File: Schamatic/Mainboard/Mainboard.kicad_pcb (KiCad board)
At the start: 2 copper layers, 45 x 120 mm, 77 parts, among them J1 CONN_01X02, J2 CONN_01X02, J3 CONN_01X02, J4 CONN_01X02, J5 CONN_01X02, J6 CONN_02X05, J7 CONN_02X20, J8 CONN_01X02, J9 CONN_01X02, Q1 Q_NMOS_GDS, Q2 PSMN014-40YS, U1 IFX91041 - 3.3V, U2 IFX91041 - 5V, U3 MC78M00, U4 LM5122, U5 UCC27611, U6 ACS781, U7 LSM6DS33, U8 STM32F031G6U6, U9 LTC2876, Y1 Resonator_Small

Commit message: 3d updates for new controller
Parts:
- added C23: 0.1uF, Capacitors_SMD:C_0603, F.Cu at (70.3, 62.1)
- added R21: 10k, Resistors_SMD:R_0603, F.Cu at (65.0, 63.3)
- moved R15 191.4 mm to (52.5, 71.6)
- moved D3 189.6 mm to (78.5, 103.0), turned to 270 degrees
- moved R16 177.6 mm to (52.6, 73.9)
- moved R17 155.6 mm to (90.5, 118.8)
- moved C2 154.2 mm to (60.2, 104.8)
- moved D1 143.2 mm to (52.9, 100.0), turned to 90 degrees
- moved R18 142.8 mm to (90.5, 120.7), turned to 180 degrees
- moved Y1 140.9 mm to (57.2, 79.9), turned to 270 degrees
- moved L1 140.9 mm to (52.8, 95.4), turned to 270 degrees
- moved C13 138.5 mm to (72.7, 92.8)
- moved L2 134.6 mm to (67.1, 94.3), turned to 90 degrees
- moved R2 111.0 mm to (57.2, 104.8)
- moved C21 110.0 mm to (90.5, 122.7), turned to 180 degrees
- moved C7 109.6 mm to (53.8, 104.9), turned to 180 degrees
- moved R3 104.5 mm to (72.3, 103.9)
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
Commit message: continue working on mainboard
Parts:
- added C24: 0.1uF, Capacitors_SMD:C_0603, F.Cu at (61.1, 64.8)
- added C25: 0.1uF, Capacitors_SMD:C_0603, F.Cu at (71.8, 72.4)
- added C26: 0.1uF, Capacitors_SMD:C_0603, F.Cu at (59.4, 73.0)
- added C27: 2.2uF, Capacitors_SMD:C_0603, F.Cu at (88.8, 106.0)
- added J10: CONN_01X04, Pin_Headers:Pin_Header_Straight_1x04_Pitch2.54mm, F.Cu at (59.8, 46.0)
- added U10: LTC2954, Dizzy:8-DFN-DDB, F.Cu at (92.8, 107.2)
- R4: value 83k -> 10k
- R5: value 10k -> 390
- moved R5 94.8 mm to (62.4, 49.5), turned to 270 degrees
- moved R4 51.1 mm to (90.9, 105.8), turned to 270 degrees
- moved C7 25.9 mm to (77.6, 94.9), turned to 270 degrees
- moved D3 23.6 mm to (54.9, 103.4), turned to 180 degrees
- moved J9 22.6 mm to (52.2, 84.9), turned to 0 degrees
- moved D1 22.1 mm to (73.7, 92.5), turned to 0 degrees
- moved R2 20.7 mm to (78.0, 104.8), turned to 180 degrees
- moved C9 19.6 mm to (58.5, 103.4), turned to 180 degrees
- moved C2 17.8 mm to (78.0, 103.2)
- moved U1 17.2 mm to (75.1, 99.5), turned to 180 degrees
- moved J6 17.0 mm to (77.7, 65.1)
- moved L1 16.5 mm to (69.2, 97.4), turned to 90 degrees
- moved C12 15.8 mm to (73.4, 95.1)
- moved C13 15.0 mm to (57.8, 94.7)
- moved J1 14.1 mm to (80.8, 46.0)
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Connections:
- J7 pad 16: (no net) -> GPIO16
- J7 pad 18: (no net) -> GPIO18
- J7 pad 33: GPIO13 -> (no net)
- J7 pad 38: GPIO20 -> PWR_INT
- J7 pad 40: GPIO21 -> ~PWR_KILL
- R4 pad 1: +BATT -> 3.3V
- R4 pad 2: Net-(R4-Pad2) -> ~PWR_KILL
- R5 pad 1: Net-(R4-Pad2) -> Net-(J10-Pad2)
- R5 pad 2: Earth -> 3.3V
- U1 pad 7: Net-(C10-Pad2) -> PWR_EN
- U2 pad 7: Net-(C9-Pad2) -> PWR_EN
- U4 pad 6: Net-(R4-Pad2) -> PWR_EN
- U8 pad 1: (no net) -> 3.3V
- U8 pad 14: GPIO13 -> V_ADC
- U8 pad 17: (no net) -> 3.3V
- U8 pad 25: GPIO21 -> GPIO18
- U8 pad 26: GPIO20 -> GPIO16
- U8 pad 6: (no net) -> I_ADC
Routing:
- net 3.3V: track 0.00 -> 263.8 mm, vias 0 -> 17
- net PWR_EN: track 0.00 -> 95.8 mm, vias 0 -> 5
- net GPIO16: track 0.00 -> 92.4 mm, vias 0 -> 4
- net +BATT: track 120.7 -> 198.9 mm, vias 4 -> 12
- net PWR_BUTTON: track 0.00 -> 75.2 mm, vias 0 -> 1
- net I_ADC: track 0.00 -> 67.2 mm, vias 0 -> 2
- net RECVRDY: track 0.00 -> 57.8 mm, vias 0 -> 2
- net V_ADC: track 0.00 -> 57.7 mm, vias 0 -> 2
- net RESPRDY: track 0.00 -> 56.7 mm, vias 0 -> 2
- net GPIO18: track 0.00 -> 43.1 mm, vias 0 -> 2
- net GPIO26: track 0.00 -> 38.9 mm
- net SCL: track 0.00 -> 38.2 mm, vias 0 -> 3
- net GPIO19: track 0.00 -> 35.7 mm
- net Net-(R17-Pad1): track 0.00 -> 34.2 mm
- net SDA: track 0.00 -> 33.9 mm, vias 0 -> 3
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- added copper zone on F.Cu, net +90V
- added copper zone on F.Cu, net +BATT
- added copper zone on B.Cu, net 3.3V
- added copper zone on F.Cu, net 3.3V
- added copper zone on B.Cu, net 5V
- added copper zone on F.Cu, net 5V
- added copper zone on B.Cu, net Earth
- added copper zone on F.Cu, net Earth
- added copper zone on F.Cu, net Net-(C15-Pad1)
- added copper zone on F.Cu, net Net-(C17-Pad1)
- added copper zone on F.Cu, net Net-(L3-Pad1)
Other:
- board size 45 x 120 mm -> 45 x 130 mm

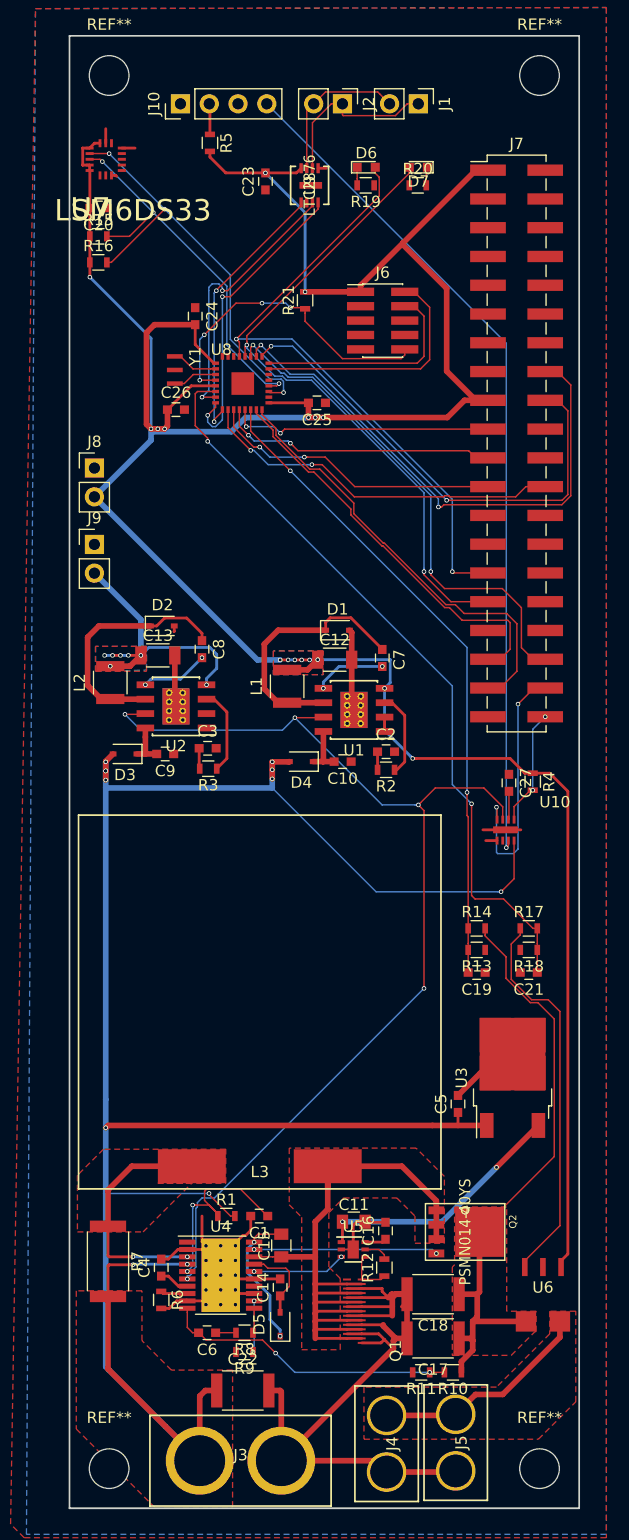
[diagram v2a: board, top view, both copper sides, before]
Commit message: bigger current regulators
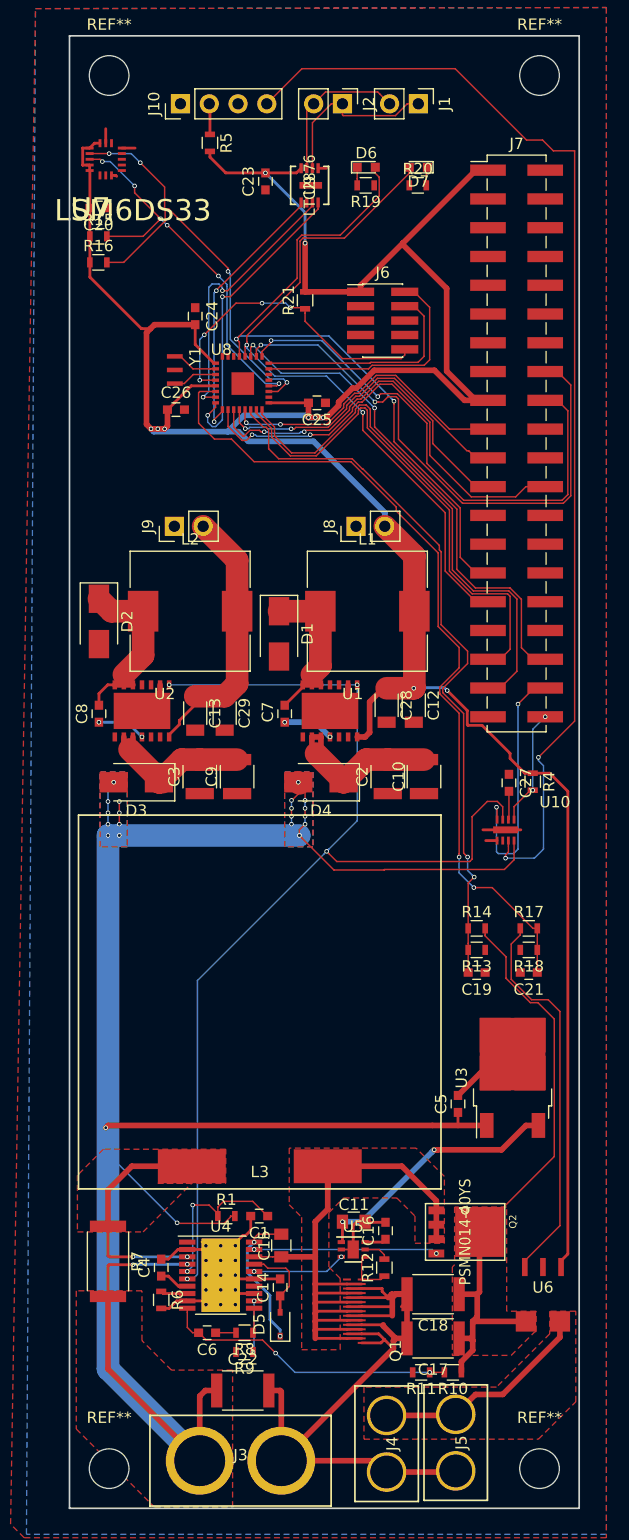
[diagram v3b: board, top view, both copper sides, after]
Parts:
- removed R2, R3: 22k, Resistors_SMD:R_0603
- added C28: 100uF, Capacitors_SMD:C_1206, F.Cu at (78.0, 99.1)
- added C29: 100uF, Capacitors_SMD:C_1206, F.Cu at (63.7, 99.8)
- C10, C9: value 1uF -> 20uF; footprint Capacitors_SMD:C_0603 -> Capacitors_SMD:C_1210
- C2, C3: value 22nF -> 20uF; footprint Capacitors_SMD:C_0603 -> Capacitors_SMD:C_1210
- C7, C8: value 0.22uF -> 0.01uF 50V
- D1, D2, D3, D4: footprint Diodes_SMD:D_SOD-323 -> Diodes_SMD:D_SMA
- L1: value 47uH -> 15uH; footprint Inductors_SMD:L_1210 -> Inductors_SMD:L_10.4x10.4_H4.8
- L2: value 47uH -> 22uH; footprint Inductors_SMD:L_1210 -> Inductors_SMD:L_10.4x10.4_H4.8
- U1: value IFX91041 - 3.3V -> LM2678-3.3V; footprint Housings_SOIC:HTSOP-8-1EP_3.9x4.9mm_Pitch1.27mm_ThermalVias -> Dizzy:14-VSON
- U2: value IFX91041 - 5V -> LM2678-5V; footprint Housings_SOIC:HTSOP-8-1EP_3.9x4.9mm_Pitch1.27mm_ThermalVias -> Dizzy:14-VSON
- moved J8 23.7 mm to (75.3, 83.3), turned to 90 degrees
- moved C8 10.7 mm to (52.6, 99.8), turned to 90 degrees
- moved C7 9.92 mm to (69.0, 99.8), turned to 90 degrees
- moved L1 9.70 mm to (76.3, 90.8), turned to 0 degrees
- moved L2 9.45 mm to (60.6, 90.8), turned to 0 degrees
- moved C12 8.06 mm to (80.4, 99.1), turned to 270 degrees
- moved C10 7.30 mm to (81.3, 105.4), turned to 90 degrees
- moved J9 7.24 mm to (59.3, 83.3), turned to 90 degrees
- moved C9 6.66 mm to (64.8, 105.4), turned to 90 degrees
- moved C13 6.07 mm to (61.1, 99.8), turned to 270 degrees
- moved D2 5.61 mm to (52.6, 91.7), turned to 270 degrees
- moved D1 5.18 mm to (68.5, 92.8), turned to 270 degrees
- moved D3 2.69 mm to (55.9, 105.9)
- moved C3 2.60 mm to (61.5, 105.4), turned to 90 degrees
- moved D4 2.52 mm to (72.2, 105.9)
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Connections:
- net GPIO18 renamed GPIO24
- C2 pad 1: Net-(C2-Pad1) -> Earth
- C2 pad 2: Earth -> Net-(C10-Pad2)
- C3 pad 1: Net-(C3-Pad1) -> Earth
- C3 pad 2: Earth -> Net-(C3-Pad2)
- C9 pad 2: Net-(C9-Pad2) -> Net-(C3-Pad2)
- D1 pad 1: Net-(C7-Pad1) -> Net-(C7-Pad2)
- D2 pad 1: Net-(C8-Pad1) -> Net-(C8-Pad2)
- D3 pad 1: Net-(C9-Pad2) -> Net-(C3-Pad2)
- J7 pad 16: GPIO16 -> GPIO23
- L1 pad 1: Net-(C7-Pad1) -> Net-(C7-Pad2)
- L2 pad 1: Net-(C8-Pad1) -> Net-(C8-Pad2)
- U1 pad 1: Earth -> (no net)
- U1 pad 2: Earth -> Net-(C10-Pad2)
- U1 pad 3: Net-(R2-Pad1) -> Net-(C10-Pad2)
- U1 pad 4: 3.3V -> Net-(C7-Pad1)
- U1 pad 5: Net-(C7-Pad2) -> (no net)
- U1 pad 6: Net-(C7-Pad1) -> (no net)
- U1 pad 7: PWR_EN -> 3.3V
- U1 pad 8: Net-(C10-Pad2) -> PWR_EN
- U2 pad 1: Earth -> (no net)
- U2 pad 2: Earth -> Net-(C3-Pad2)
- U2 pad 3: Net-(R3-Pad1) -> Net-(C3-Pad2)
- U2 pad 4: 5V -> Net-(C8-Pad1)
- U2 pad 5: Net-(C8-Pad2) -> (no net)
- U2 pad 6: Net-(C8-Pad1) -> (no net)
- U2 pad 7: PWR_EN -> 5V
- U2 pad 8: Net-(C9-Pad2) -> PWR_EN
- U8 pad 26: GPIO16 -> GPIO23
- U8 pad 33: (no net) -> Earth
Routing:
- net GPIO23: track 0.00 -> 49.6 mm, vias 0 -> 2
- net GPIO16: track 92.4 -> 45.0 mm, vias 4 -> 2
- net PWR_BUTTON: track 75.2 -> 100.0 mm, vias 1 -> 2
- net Net-(C7-Pad1): track 22.6 -> 4.54 mm, vias 0 -> 2
- net Net-(C8-Pad1): track 21.9 -> 4.34 mm, vias 0 -> 2
- net Net-(C3-Pad2): track 0.00 -> 14.9 mm
- net 3.3V: track 263.8 -> 250.0 mm, vias 17 -> 10
- net Net-(C10-Pad2): track 4.52 -> 15.6 mm
- net Net-(C8-Pad2): track 5.99 -> 15.9 mm, vias 2 -> 0
- net GPIO19: track 35.7 -> 44.6 mm
- net GPIO26: track 38.9 -> 47.4 mm
- net Earth: track 127.4 -> 118.9 mm
- net Net-(C7-Pad2): track 6.32 -> 14.5 mm, vias 2 -> 0
- net Net-(R3-Pad1): track 7.64 -> 0.00 mm
- net Net-(R2-Pad1): track 7.54 -> 0.00 mm
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- added copper zone on B.Cu, net +BATT
- removed copper zone on B.Cu, net 3.3V
- removed copper zone on F.Cu, net 3.3V
- removed copper zone on B.Cu, net 5V
- removed copper zone on F.Cu, net 5V

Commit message: progress
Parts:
- added ?: , Dizzy:2x2mm-pad, F.Cu at (55.9, 138.8)
- added ?: , Dizzy:2x2mm-pad, F.Cu at (87.2, 151.2)
- added ?: , Dizzy:2x2mm-pad, F.Cu at (93.0, 156.1)
- added ?: , Dizzy:2x2mm-pad, F.Cu at (91.0, 159.6)
- added ?: , Dizzy:2x2mm-pad, F.Cu at (81.2, 160.6)
- added ?: , Dizzy:2x2mm-pad, F.Cu at (78.0, 153.6)
- added ?: , Dizzy:2x2mm-pad, F.Cu at (78.1, 150.4)
- added ?: , Dizzy:2x2mm-pad, F.Cu at (70.5, 158.8)
- added ?: , Dizzy:2x2mm-pad, F.Cu at (81.0, 165.7)
- added ?: , Dizzy:2x2mm-pad, F.Cu at (73.8, 165.3)
- added ?: , Dizzy:2x2mm-pad, F.Cu at (73.7, 161.4)
- added ?: , Dizzy:2x2mm-pad, F.Cu at (55.9, 141.4)
- added ?: , Dizzy:2x2mm-pad, F.Cu at (57.0, 163.5)
- added ?: , Dizzy:2x2mm-pad, F.Cu at (60.5, 159.1)
- added ?: , Dizzy:2x2mm-pad, F.Cu at (56.5, 159.5)
- added ?: , Dizzy:2x2mm-pad, F.Cu at (53.5, 159.7)
- added ?: , Dizzy:2x2mm-pad, F.Cu at (53.5, 156.0)
- added ?: , Dizzy:2x2mm-pad, F.Cu at (53.5, 152.8)
- added ?: , Dizzy:2x2mm-pad, F.Cu at (73.5, 158.5)
- added ?: , Dizzy:2x2mm-pad, F.Cu at (87.8, 160.2)
- added ?: , Dizzy:2x2mm-pad, F.Cu at (87.2, 153.7)
- added ?: , Dizzy:2x2mm-pad, F.Cu at (77.6, 138.4)
- added ?: , Dizzy:2x2mm-pad, F.Cu at (72.2, 152.7)
- added ?: , Dizzy:2x2mm-pad, F.Cu at (52.6, 141.4)
- added ?: , Dizzy:2x2mm-pad, F.Cu at (72.0, 149.2)
- added ?: , Dizzy:2x2mm-pad, F.Cu at (71.8, 145.6)
- added ?: , Dizzy:2x2mm-pad, F.Cu at (71.7, 141.6)
- added ?: , Dizzy:2x2mm-pad, F.Cu at (81.5, 141.0)
- added ?: , Dizzy:2x2mm-pad, F.Cu at (80.0, 138.7)
- added ?: , Dizzy:2x2mm-pad, F.Cu at (87.2, 148.4)
- added REF**: VIA-0.4, Dizzy:VIA-0.4, F.Cu at (70.8, 71.2)
- added REF**: VIA-0.4, Dizzy:VIA-0.4, F.Cu at (51.2, 129.3)
- added REF**: VIA-0.4, Dizzy:VIA-0.4, F.Cu at (54.8, 98.8)
- added REF**: VIA-0.4, Dizzy:VIA-0.4, F.Cu at (55.6, 98.8)
- added REF**: VIA-0.4, Dizzy:VIA-0.4, F.Cu at (56.5, 98.9)
- added REF**: VIA-0.4, Dizzy:VIA-0.4, F.Cu at (57.4, 98.9)
- added REF**: VIA-0.4, Dizzy:VIA-0.4, F.Cu at (58.2, 98.9)
- added REF**: VIA-0.4, Dizzy:VIA-0.4, F.Cu at (75.0, 100.4)
- added REF**: VIA-0.4, Dizzy:VIA-0.4, F.Cu at (74.3, 100.5)
- added REF**: VIA-0.4, Dizzy:VIA-0.4, F.Cu at (73.6, 100.5)
- added REF**: VIA-0.4, Dizzy:VIA-0.4, F.Cu at (72.8, 100.5)
- added REF**: VIA-0.4, Dizzy:VIA-0.4, F.Cu at (71.8, 100.5)
- added REF**: VIA-0.4, Dizzy:VIA-0.4, F.Cu at (51.2, 123.8)
- added REF**: VIA-0.4, Dizzy:VIA-0.4, F.Cu at (71.1, 100.5)
- added REF**: VIA-0.4, Dizzy:VIA-0.4, F.Cu at (71.2, 99.5)
- added REF**: VIA-0.4, Dizzy:VIA-0.4, F.Cu at (71.9, 99.5)
- added REF**: VIA-0.4, Dizzy:VIA-0.4, F.Cu at (72.8, 99.5)
- added REF**: VIA-0.4, Dizzy:VIA-0.4, F.Cu at (73.7, 99.5)
- added REF**: VIA-0.4, Dizzy:VIA-0.4, F.Cu at (74.3, 99.5)
- added REF**: VIA-0.4, Dizzy:VIA-0.4, F.Cu at (75.2, 99.5)
- added REF**: VIA-0.4, Dizzy:VIA-0.4, F.Cu at (75.2, 98.7)
- added REF**: VIA-0.4, Dizzy:VIA-0.4, F.Cu at (74.5, 98.7)
- added REF**: VIA-0.4, Dizzy:VIA-0.4, F.Cu at (73.8, 98.7)
- added REF**: VIA-0.4, Dizzy:VIA-0.4, F.Cu at (51.3, 118.6)
- added REF**: VIA-0.4, Dizzy:VIA-0.4, F.Cu at (72.8, 98.7)
- added REF**: VIA-0.4, Dizzy:VIA-0.4, F.Cu at (71.8, 98.7)
- added REF**: VIA-0.4, Dizzy:VIA-0.4, F.Cu at (71.1, 98.7)
- added REF**: VIA-0.4, Dizzy:VIA-0.4, F.Cu at (87.0, 82.5)
- added REF**: VIA-0.4, Dizzy:VIA-0.4, F.Cu at (89.7, 86.3)
- added REF**: VIA-0.4, Dizzy:VIA-0.4, F.Cu at (92.1, 87.5)
- added REF**: VIA-0.4, Dizzy:VIA-0.4, F.Cu at (92.0, 92.5)
- added REF**: VIA-0.4, Dizzy:VIA-0.4, F.Cu at (88.3, 100.1)
- added REF**: VIA-0.4, Dizzy:VIA-0.4, F.Cu at (87.0, 100.1)
- added REF**: VIA-0.4, Dizzy:VIA-0.4, F.Cu at (87.5, 104.8)
- added REF**: VIA-0.4, Dizzy:VIA-0.4, F.Cu at (51.2, 115.7)
- added REF**: VIA-0.4, Dizzy:VIA-0.4, F.Cu at (86.6, 103.6)
- added REF**: VIA-0.4, Dizzy:VIA-0.4, F.Cu at (86.4, 104.8)
- added REF**: VIA-0.4, Dizzy:VIA-0.4, F.Cu at (82.1, 110.8)
- added REF**: VIA-0.4, Dizzy:VIA-0.4, F.Cu at (80.4, 109.3)
- added REF**: VIA-0.4, Dizzy:VIA-0.4, F.Cu at (77.9, 109.5)
- added REF**: VIA-0.4, Dizzy:VIA-0.4, F.Cu at (76.9, 111.2)
- added REF**: VIA-0.4, Dizzy:VIA-0.4, F.Cu at (92.0, 114.0)
- added REF**: VIA-0.4, Dizzy:VIA-0.4, F.Cu at (90.5, 115.2)
- added REF**: VIA-0.4, Dizzy:VIA-0.4, F.Cu at (92.0, 116.2)
- added REF**: VIA-0.4, Dizzy:VIA-0.4, F.Cu at (92.8, 123.8)
- added REF**: VIA-0.4, Dizzy:VIA-0.4, F.Cu at (51.2, 113.5)
- added REF**: VIA-0.4, Dizzy:VIA-0.4, F.Cu at (89.9, 122.7)
- added REF**: VIA-0.4, Dizzy:VIA-0.4, F.Cu at (70.6, 120.0)
- added REF**: VIA-0.4, Dizzy:VIA-0.4, F.Cu at (67.8, 123.7)
- added REF**: VIA-0.4, Dizzy:VIA-0.4, F.Cu at (69.0, 128.8)
- added REF**: VIA-0.4, Dizzy:VIA-0.4, F.Cu at (68.7, 132.4)
- added REF**: VIA-0.4, Dizzy:VIA-0.4, F.Cu at (76.0, 131.7)
- added REF**: VIA-0.4, Dizzy:VIA-0.4, F.Cu at (76.5, 127.5)
- added REF**: VIA-0.4, Dizzy:VIA-0.4, F.Cu at (76.6, 124.1)
- added REF**: VIA-0.4, Dizzy:VIA-0.4, F.Cu at (78.0, 118.2)
- added REF**: VIA-0.4, Dizzy:VIA-0.4, F.Cu at (81.1, 119.0)
- added REF**: VIA-0.4, Dizzy:VIA-0.4, F.Cu at (66.3, 108.3)
- added REF**: VIA-0.4, Dizzy:VIA-0.4, F.Cu at (76.8, 121.0)
- added REF**: VIA-0.4, Dizzy:VIA-0.4, F.Cu at (81.4, 122.7)
- added REF**: VIA-0.4, Dizzy:VIA-0.4, F.Cu at (81.5, 129.1)
- added REF**: VIA-0.4, Dizzy:VIA-0.4, F.Cu at (81.4, 133.1)
- added REF**: VIA-0.4, Dizzy:VIA-0.4, F.Cu at (81.2, 153.1)
- added REF**: VIA-0.4, Dizzy:VIA-0.4, F.Cu at (82.5, 153.2)
- added REF**: VIA-0.4, Dizzy:VIA-0.4, F.Cu at (82.5, 155.0)
- added REF**: VIA-0.4, Dizzy:VIA-0.4, F.Cu at (81.2, 155.0)
- added REF**: VIA-0.4, Dizzy:VIA-0.4, F.Cu at (82.4, 151.1)
- added REF**: VIA-0.4, Dizzy:VIA-0.4, F.Cu at (81.4, 151.1)
- added REF**: VIA-0.4, Dizzy:VIA-0.4, F.Cu at (61.8, 108.5)
- added REF**: VIA-0.4, Dizzy:VIA-0.4, F.Cu at (92.0, 151.2)
- added REF**: VIA-0.4, Dizzy:VIA-0.4, F.Cu at (92.0, 150.2)
- added REF**: VIA-0.4, Dizzy:VIA-0.4, F.Cu at (87.5, 127.7)
- added REF**: VIA-0.4, Dizzy:VIA-0.4, F.Cu at (58.4, 108.5)
- added REF**: VIA-0.4, Dizzy:VIA-0.4, F.Cu at (67.8, 103.0)
- added REF**: VIA-0.4, Dizzy:VIA-0.4, F.Cu at (67.6, 98.2)
- added REF**: VIA-0.4, Dizzy:VIA-0.4, F.Cu at (72.0, 71.2)
- added REF**: VIA-0.4, Dizzy:VIA-0.4, F.Cu at (76.4, 92.5)
- added REF**: VIA-0.4, Dizzy:VIA-0.4, F.Cu at (76.7, 87.5)
- added REF**: VIA-0.4, Dizzy:VIA-0.4, F.Cu at (59.6, 87.5)
- added REF**: VIA-0.4, Dizzy:VIA-0.4, F.Cu at (60.5, 92.3)
- added REF**: VIA-0.4, Dizzy:VIA-0.4, F.Cu at (69.1, 84.3)
- added REF**: VIA-0.4, Dizzy:VIA-0.4, F.Cu at (70.3, 80.3)
- added REF**: VIA-0.4, Dizzy:VIA-0.4, F.Cu at (66.5, 82.2)
- added REF**: VIA-0.4, Dizzy:VIA-0.4, F.Cu at (62.0, 79.8)
- added REF**: VIA-0.4, Dizzy:VIA-0.4, F.Cu at (59.1, 80.0)
- added REF**: VIA-0.4, Dizzy:VIA-0.4, F.Cu at (64.5, 78.4)
- added REF**: VIA-0.4, Dizzy:VIA-0.4, F.Cu at (72.7, 72.3)
- added REF**: VIA-0.4, Dizzy:VIA-0.4, F.Cu at (61.0, 77.3)
- added REF**: VIA-0.4, Dizzy:VIA-0.4, F.Cu at (57.4, 78.0)
- added REF**: VIA-0.4, Dizzy:VIA-0.4, F.Cu at (54.8, 68.3)
- added REF**: VIA-0.4, Dizzy:VIA-0.4, F.Cu at (54.5, 72.5)
- added REF**: VIA-0.4, Dizzy:VIA-0.4, F.Cu at (54.8, 76.3)
- added REF**: VIA-0.4, Dizzy:VIA-0.4, F.Cu at (54.5, 79.0)
- added REF**: VIA-0.4, Dizzy:VIA-0.4, F.Cu at (54.8, 82.8)
- added REF**: VIA-0.4, Dizzy:VIA-0.4, F.Cu at (52.2, 84.3)
- added REF**: VIA-0.4, Dizzy:VIA-0.4, F.Cu at (52.4, 80.0)
- added REF**: VIA-0.4, Dizzy:VIA-0.4, F.Cu at (52.4, 74.8)
- added REF**: VIA-0.4, Dizzy:VIA-0.4, F.Cu at (87.0, 62.1)
- added REF**: VIA-0.4, Dizzy:VIA-0.4, F.Cu at (52.4, 69.6)
- added REF**: VIA-0.4, Dizzy:VIA-0.4, F.Cu at (52.4, 65.7)
- added REF**: VIA-0.4, Dizzy:VIA-0.4, F.Cu at (57.6, 61.0)
- added REF**: VIA-0.4, Dizzy:VIA-0.4, F.Cu at (59.6, 60.8)
- added REF**: VIA-0.4, Dizzy:VIA-0.4, F.Cu at (56.1, 62.3)
- added REF**: VIA-0.4, Dizzy:VIA-0.4, F.Cu at (58.9, 62.4)
- added REF**: VIA-0.4, Dizzy:VIA-0.4, F.Cu at (58.4, 59.7)
- added REF** (x2): VIA-0.4, Dizzy:VIA-0.4, F.Cu at (53.3, 53.9)
- added REF**: VIA-0.4, Dizzy:VIA-0.4, F.Cu at (54.4, 54.4)
- added REF**: VIA-0.4, Dizzy:VIA-0.4, F.Cu at (92.1, 57.0)
- added REF**: VIA-0.4, Dizzy:VIA-0.4, F.Cu at (55.0, 55.9)
- added REF**: VIA-0.4, Dizzy:VIA-0.4, F.Cu at (86.5, 41.5)
- added REF**: VIA-0.4, Dizzy:VIA-0.4, F.Cu at (82.3, 41.4)
- added REF**: VIA-0.4, Dizzy:VIA-0.4, F.Cu at (76.5, 41.4)
- added REF**: VIA-0.4, Dizzy:VIA-0.4, F.Cu at (68.5, 41.5)
- added REF**: VIA-0.4, Dizzy:VIA-0.4, F.Cu at (64.1, 42.1)
- added REF**: VIA-0.4, Dizzy:VIA-0.4, F.Cu at (59.8, 42.0)
- added REF**: VIA-0.4, Dizzy:VIA-0.4, F.Cu at (56.2, 47.6)
- added REF**: VIA-0.4, Dizzy:VIA-0.4, F.Cu at (69.2, 48.8)
- added REF**: VIA-0.4, Dizzy:VIA-0.4, F.Cu at (66.7, 49.4)
- added REF**: VIA-0.4, Dizzy:VIA-0.4, F.Cu at (84.0, 56.5)
- added REF**: VIA-0.4, Dizzy:VIA-0.4, F.Cu at (58.5, 49.8)
- added REF**: VIA-0.4, Dizzy:VIA-0.4, F.Cu at (60.5, 51.9)
- added REF**: VIA-0.4, Dizzy:VIA-0.4, F.Cu at (63.1, 54.7)
- added REF**: VIA-0.4, Dizzy:VIA-0.4, F.Cu at (65.3, 54.6)
- added REF**: VIA-0.4, Dizzy:VIA-0.4, F.Cu at (66.3, 56.2)
- added REF**: VIA-0.4, Dizzy:VIA-0.4, F.Cu at (64.5, 58.1)
- added REF**: VIA-0.4, Dizzy:VIA-0.4, F.Cu at (87.2, 49.0)
- added REF**: VIA-0.4, Dizzy:VIA-0.4, F.Cu at (85.0, 46.0)
- added REF**: VIA-0.4, Dizzy:VIA-0.4, F.Cu at (83.8, 48.9)
- added REF**: VIA-0.4, Dizzy:VIA-0.4, F.Cu at (81.7, 49.2)
- added REF**: VIA-0.4, Dizzy:VIA-0.4, F.Cu at (83.6, 59.4)
- added REF**: VIA-0.4, Dizzy:VIA-0.4, F.Cu at (79.5, 49.1)
- added REF**: VIA-0.4, Dizzy:VIA-0.4, F.Cu at (76.9, 49.0)
- added REF**: VIA-0.4, Dizzy:VIA-0.4, F.Cu at (73.8, 49.0)
- added REF**: VIA-0.4, Dizzy:VIA-0.4, F.Cu at (73.8, 51.5)
- added REF**: VIA-0.4, Dizzy:VIA-0.4, F.Cu at (74.0, 53.1)
- added REF**: VIA-0.4, Dizzy:VIA-0.4, F.Cu at (73.8, 55.5)
- added REF**: VIA-0.4, Dizzy:VIA-0.4, F.Cu at (73.2, 59.9)
- added REF**: VIA-0.4, Dizzy:VIA-0.4, F.Cu at (75.4, 59.1)
- added REF**: VIA-0.4, Dizzy:VIA-0.4, F.Cu at (77.2, 57.5)
- added REF**: VIA-0.4, Dizzy:VIA-0.4, F.Cu at (78.5, 56.7)
- added REF**: VIA-0.4, Dizzy:VIA-0.4, F.Cu at (83.1, 58.1)
- added REF**: VIA-0.4, Dizzy:VIA-0.4, F.Cu at (80.0, 54.7)
- added REF**: VIA-0.4, Dizzy:VIA-0.4, F.Cu at (75.8, 67.7)
- added REF**: VIA-0.4, Dizzy:VIA-0.4, F.Cu at (75.8, 63.9)
- added REF**: VIA-0.4, Dizzy:VIA-0.4, F.Cu at (65.3, 70.0)
- added REF**: VIA-0.4, Dizzy:VIA-0.4, F.Cu at (65.3, 71.2)
- added REF**: VIA-0.4, Dizzy:VIA-0.4, F.Cu at (65.9, 70.7)
- added REF**: VIA-0.4, Dizzy:VIA-0.4, F.Cu at (64.8, 70.7)
- added REF**: VIA-0.4, Dizzy:VIA-0.4, F.Cu at (65.3, 70.7)
- added REF**: VIA-0.4, Dizzy:VIA-0.4, F.Cu at (54.6, 100.3)
- added REF**: VIA-0.4, Dizzy:VIA-0.4, F.Cu at (55.5, 100.3)
- added REF**: VIA-0.4, Dizzy:VIA-0.4, F.Cu at (51.5, 103.2)
- added REF**: VIA-0.4, Dizzy:VIA-0.4, F.Cu at (56.4, 100.3)
- added REF**: VIA-0.4, Dizzy:VIA-0.4, F.Cu at (57.1, 100.3)
- added REF**: VIA-0.4, Dizzy:VIA-0.4, F.Cu at (57.7, 100.4)
- added REF**: VIA-0.4, Dizzy:VIA-0.4, F.Cu at (58.6, 100.5)
- added REF**: VIA-0.4, Dizzy:VIA-0.4, F.Cu at (58.6, 99.5)
- added REF**: VIA-0.4, Dizzy:VIA-0.4, F.Cu at (57.9, 99.5)
- added REF**: VIA-0.4, Dizzy:VIA-0.4, F.Cu at (57.1, 99.5)
- added REF**: VIA-0.4, Dizzy:VIA-0.4, F.Cu at (56.4, 99.5)
- added REF**: VIA-0.4, Dizzy:VIA-0.4, F.Cu at (55.5, 99.6)
- added REF**: VIA-0.4, Dizzy:VIA-0.4, F.Cu at (54.6, 99.6)
- C12, C13, C28, C29: footprint Capacitors_SMD:C_1206 -> Capacitors_SMD:C_1210
- C17, C18: value C -> 3.3uF
- C22: value 2uF -> 4.7uF
- moved C12 0.75 mm to (81.2, 99.1)
- moved C29 0.65 mm to (64.3, 99.8)
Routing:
- net Earth: track 118.9 -> 121.4 mm
- net DE: track 24.1 -> 24.6 mm
